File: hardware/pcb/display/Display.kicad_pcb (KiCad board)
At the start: 2 copper layers, 48 x 26 mm, 6 parts, among them J1 Conn_01x05, U3 74HC595, U4 HD44780

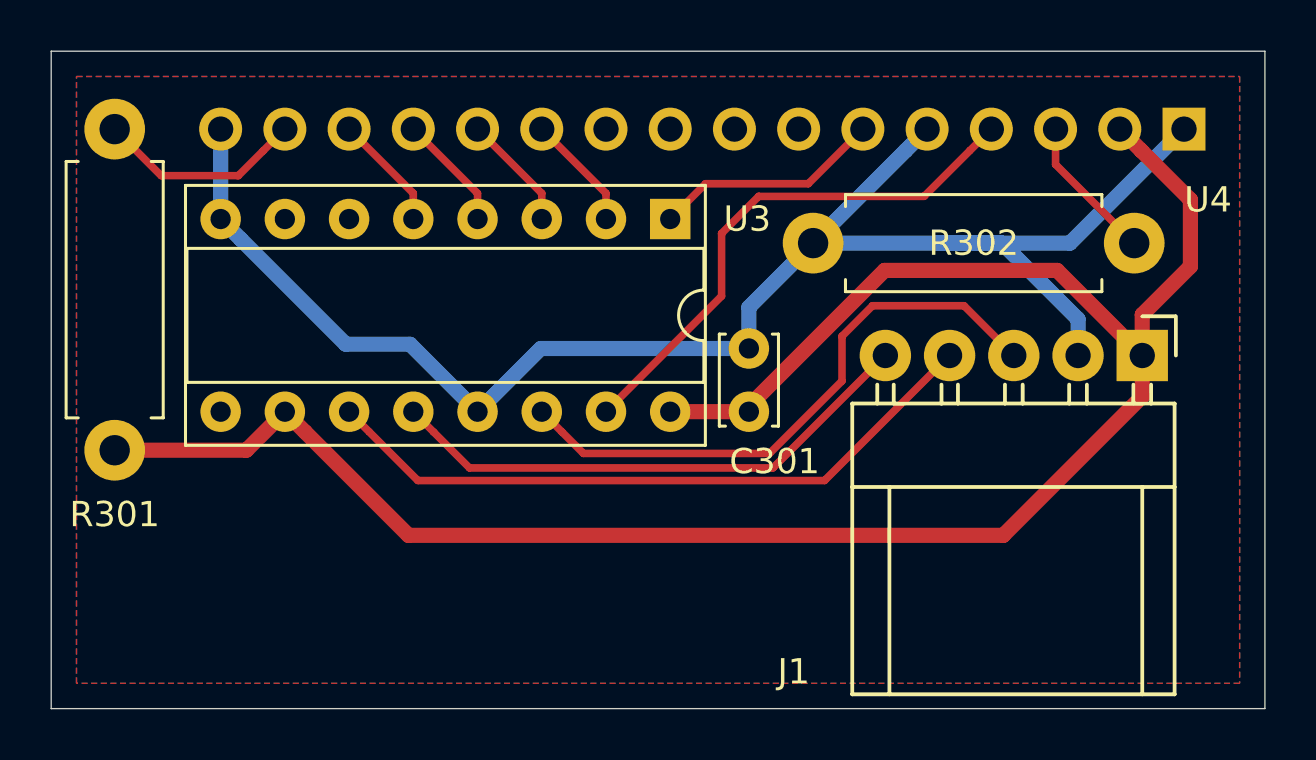
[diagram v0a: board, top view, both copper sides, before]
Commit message: feat: Split Display SPI converter from main PCB
shrink display connector

Issue #13
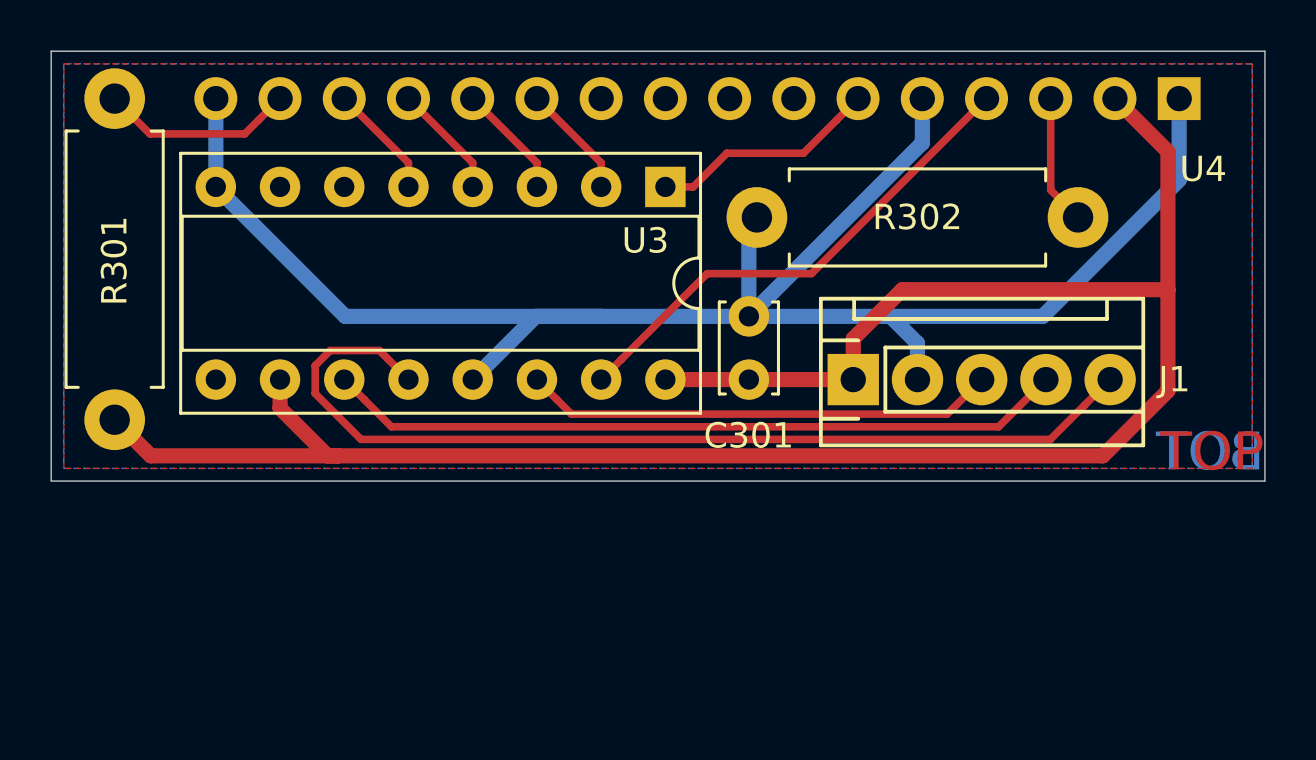
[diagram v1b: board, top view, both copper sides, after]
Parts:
- J1: footprint Molex:Molex_KK256_Pin_Header_Angled_1x05 -> Molex:Molex_KK256_Pin_Header_Straight_1x05
- moved J1 11.5 mm to (45.7, 27.0), turned to 90 degrees
- moved R302 2.44 mm to (54.6, 20.6)
- moved U3 1.28 mm to (38.3, 19.4)
- moved C301 1.27 mm to (41.6, 27.0)
- moved U4 1.22 mm to (58.6, 15.9)
- moved R301 1.21 mm to (16.5, 28.6)
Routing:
- net /CS2: track 21.4 -> 38.7 mm
- net GND: track 65.1 -> 73.7 mm
- net /MOSI: track 23.6 -> 18.7 mm
- net /SCLK: track 26.9 -> 29.3 mm
- net +5V: track 80.6 -> 82.3 mm
- net /RS: track 21.3 -> 19.8 mm
- net Net-(R302-Pad1): track 5.80 -> 5.15 mm
- net Net-(R301-Pad2): track 8.26 -> 7.70 mm
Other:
- board size 48 x 26 mm -> 48 x 17 mm
- board text added: "BOT"
- board text added: "TOP"
